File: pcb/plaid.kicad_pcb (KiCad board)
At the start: 2 copper layers, 228 x 98 mm, 139 parts, among them J1 USB_OTG, J2 AVR_ISP_6, J3 Conn_01x04, J4 GS2, J5 GS2, SW1 SW_Push, SW10 SW_Push, SW11 SW_Push, SW12 SW_Push, SW13 SW_Push, SW14 SW_Push, SW15 SW_Push, SW16 SW_Push, SW17 SW_Push, SW18 SW_Push, SW19 SW_Push, SW2 SW_Push, SW20 SW_Push, SW21 SW_Push, SW22 SW_Push, SW23 SW_Push, SW24 SW_Push, SW25 SW_Push, SW26 SW_Push, SW27 SW_Push, SW28 SW_Push, SW29 SW_Push, SW3 SW_Push, SW30 SW_Push, SW31 SW_Push, SW32 SW_Push, SW33 SW_Push, SW34 SW_Push, SW35 SW_Push, SW36 SW_Push, SW37 SW_Push, SW38 SW_Push, SW39 SW_Push, SW4 SW_Push, SW40 SW_Push, SW41 SW_Push, SW42 SW_Push, SW43 SW_Push, SW44 SW_Push, SW45 SW_Push, SW46 SW_Push, SW47 SW_Push, SW48 SW_Push, SW49 SW_Push, SW5 SW_Push, SW50 RESET, SW51 BOOT, SW6 SW_Push, SW7 SW_Push, SW8 SW_Push, SW9 SW_Push, U1 ATMEGA328-PU, Y1 16MHz

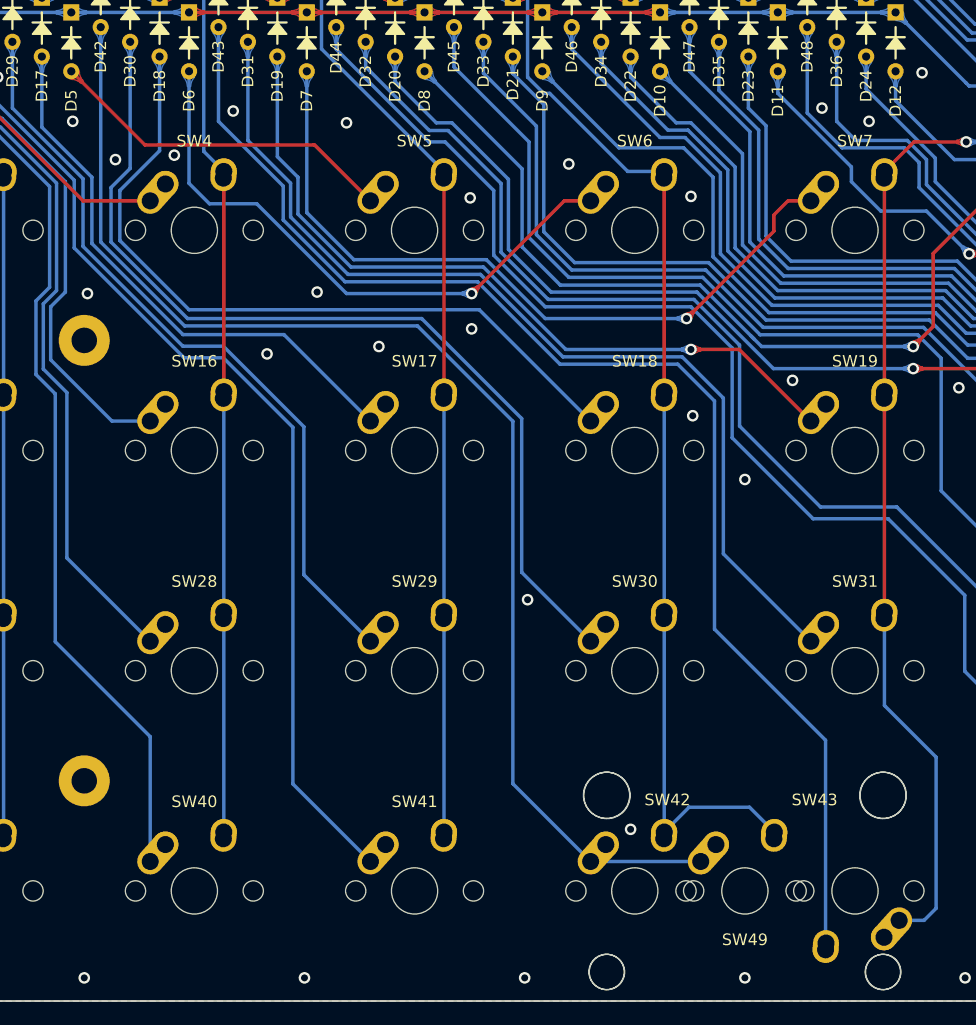
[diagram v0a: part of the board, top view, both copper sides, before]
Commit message: cleaned up Alps supported design
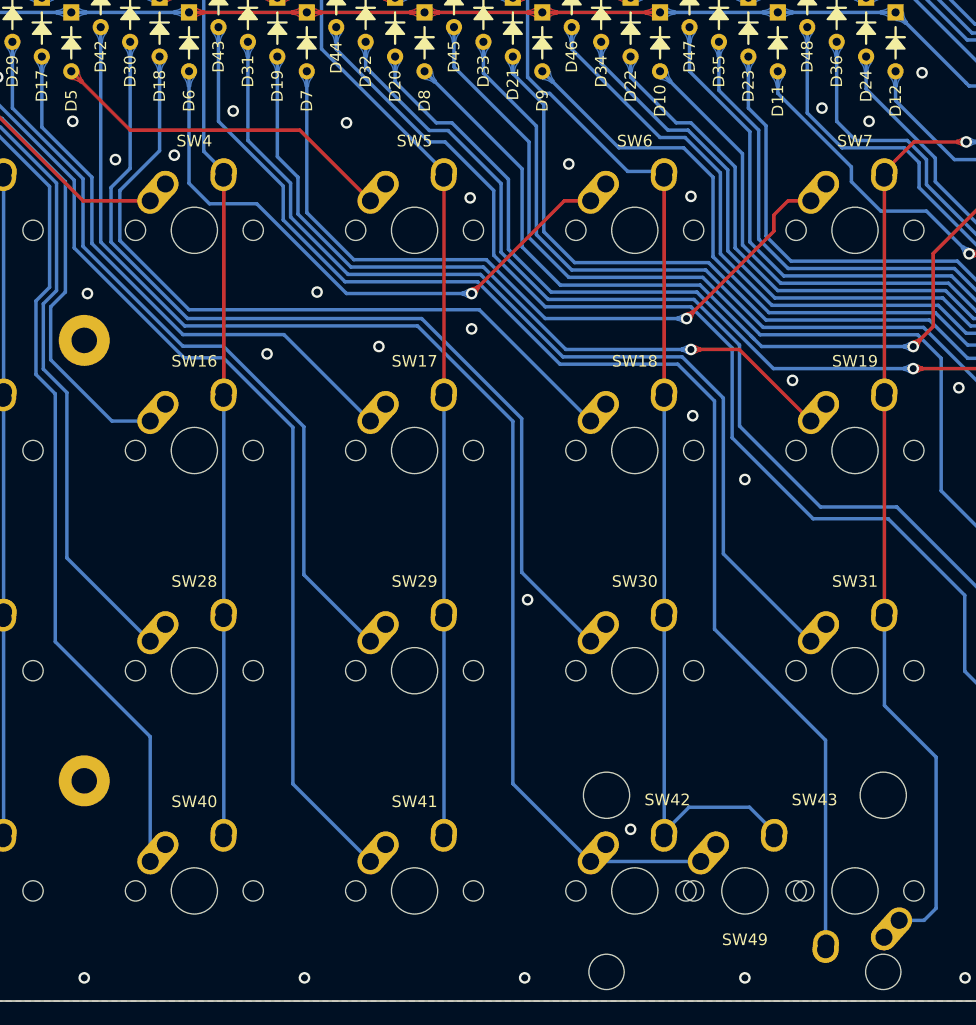
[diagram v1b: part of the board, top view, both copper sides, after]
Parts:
- removed REF**: Stab_MX_2u, SMKJP:Stab_MX_2u
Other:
- board text added: "Plaid // Through Hole // Rev.1 (c)2019 Takuya Urakawa, Dm9Records.com Alps support added by /u/emdarcher"
- board text removed: "Plaid // Through Hole // Rev.1 (c)2019 Takuya Urakawa, Dm9Records.com"
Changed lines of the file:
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@@
     (tracks 885)
     (zones 0)
-    (modules 139)
+    (modules 138)
     (nets 81)
   )
@@
       (layerselection 0x010f0_ffffffff)
       (usegerberextensions true)
-      (usegerberattributes false)
+      (usegerberattributes true)
       (usegerberadvancedattributes false)
       (creategerberjobfile false)
@@
       (net 60 /COL5))
   )
-  (module SMKJP:Stab_MX_2u (layer F.Cu)
-    (at 164 138.5 180)
-    (descr "Cherry MX keyswitch, MX1A, 2.00u, PCB mount, http://cherryamericas.com/wp-content/uploads/2014/12/mx_cat.pdf")
-    (tags "cherry mx keyswitch MX1A 2.00u PCB")
-    (fp_text reference REF** (at 0 -7.874 180) (layer F.SilkS) hide
-      (effects (font (size 1 1) (thickness 0.15)))
-    )
-    (fp_text value Stab_MX_2u (at 0 7.874 180) (layer F.Fab)
-      (effects (font (size 1 1) (thickness 0.15)))
-    )
-    (fp_line (start -7 7) (end -7 -7) (layer F.Fab) (width 0.1))
-    (fp_line (start 7 7) (end -7 7) (layer F.Fab) (width 0.1))
-    (fp_line (start 7 -7) (end 7 7) (layer F.Fab) (width 0.1))
-    (fp_line (start -7 -7) (end 7 -7) (layer F.Fab) (width 0.1))
-    (fp_line (start -19.05 9.525) (end -19.05 -9.525) (layer Dwgs.User) (width 0.15))
-    (fp_line (start 19.05 9.525) (end -19.05 9.525) (layer Dwgs.User) (width 0.15))
-    (fp_line (start 19.05 -9.525) (end 19.05 9.525) (layer Dwgs.User) (width 0.15))
-    (fp_line (start -19.05 -9.525) (end 19.05 -9.525) (layer Dwgs.User) (width 0.15))
-    (fp_text user %R (at 0 -7.874 180) (layer F.Fab)
-      (effects (font (size 1 1) (thickness 0.15)))
-    )
-    (pad "" np_thru_hole circle (at 11.9 -7 180) (size 3.05 3.05) (drill 3.05) (layers *.Cu *.Mask))
-    (pad "" np_thru_hole circle (at -11.9 -7 180) (size 3.05 3.05) (drill 3.05) (layers *.Cu *.Mask))
-    (pad "" np_thru_hole circle (at -11.9 8.24 180) (size 4 4) (drill 4) (layers *.Cu *.Mask))
-    (pad "" np_thru_hole circle (at 11.9 8.24 180) (size 4 4) (drill 4) (layers *.Cu *.Mask))
-    (model ${KISYS3DMOD}/Buttons_Switches_Keyboard.3dshapes/SW_Cherry_MX1A_2.00u_PCB.wrl
-      (at (xyz 0 0 0))
-      (scale (xyz 1 1 1))
-      (rotate (xyz 0 0 0))
-    )
-  )
   (module MX_Alps_Hybrid:MX-1U-NoLED_edit_no_Fsilk (layer F.Cu)
     (at 154.5 138.5)
@@
   (gr_line (start 254.216 62.7) (end 254.216 66.51) (layer B.SilkS) (width 0.2))
   (gr_line (start 254.978 62.7) (end 254.216 62.7) (layer B.SilkS) (width 0.2))
-  (gr_text "Plaid // Through Hole // Rev.1\n(c)2019 Takuya Urakawa, Dm9Records.com" (at 273.901 127.47) (layer B.SilkS)
+  (gr_text "Plaid // Through Hole // Rev.1\n(c)2019 Takuya Urakawa, Dm9Records.com\nAlps support added by /u/emdarcher" (at 273.901 126.835) (layer B.SilkS)
     (effects (font (size 1.5 1.5) (thickness 0.25)) (justify left mirror))
   )
@@
   (segment (start 106.9 78.96) (end 112.69 78.96) (width 0.3) (layer F.Cu) (net 5) (status 20))
   (segment (start 95.72 67.78) (end 106.9 78.96) (width 0.3) (layer F.Cu) (net 5) (status 10))
-  (segment (start 126.86 74.13) (end 131.69 78.96) (width 0.3) (layer F.Cu) (net 6) (status 20))
-  (segment (start 105.88 67.78) (end 112.23 74.13) (width 0.3) (layer F.Cu) (net 6) (status 10))
-  (segment (start 112.23 74.13) (end 126.86 74.13) (width 0.3) (layer F.Cu) (net 6))
+  (segment (start 125.59 72.86) (end 131.69 78.96) (width 0.3) (layer F.Cu) (net 6))
+  (segment (start 110.96 72.86) (end 125.59 72.86) (width 0.3) (layer F.Cu) (net 6))
+  (segment (start 105.88 67.78) (end 110.96 72.86) (width 0.3) (layer F.Cu) (net 6))
   (via (at 140.424 86.957) (size 1) (drill 0.6) (layers F.Cu B.Cu) (net 7))
   (segment (start 148.421 78.96) (end 150.69 78.96) (width 0.3) (layer F.Cu) (net 7) (status 20))
